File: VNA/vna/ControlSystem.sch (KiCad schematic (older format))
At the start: 2 parts

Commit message: block diagram for presentation completed
at this stage i have completed the overall block diagram for the initial presentation.

the blocks are mostly empty and require further development. the overall block diagram neglects power supply connections for clarity, these will be added internal to the blocks.
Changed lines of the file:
@@
 $Descr A4 11693 8268
 encoding utf-8
-Sheet 8 9
+Sheet 10 10
 Title ""
 Date ""
@@
 Text HLabel 6650 1500 1    50   Input ~ 0
 Aref
+Text HLabel 4800 2000 0    50   Input ~ 0
+VmagIn
+Text HLabel 4800 2200 0    50   Input ~ 0
+VphaseIn
+Text HLabel 4800 2450 0    50   Input ~ 0
+VrefIn
+Text HLabel 4800 2650 0    50   Input ~ 0
+DataNegIn
+Text HLabel 4800 2900 0    50   Input ~ 0
+DataPosIn
+Text HLabel 4800 3150 0    50   Input ~ 0
+SrcCtlOut
+Text HLabel 4800 3300 0    50   Input ~ 0
+ACtrlOut
+Text HLabel 4800 3450 0    50   Input ~ 0
+BCtrlOut
+Text HLabel 4800 1750 0    50   Input ~ 0
+RFControl
 $EndSCHEMATC

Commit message: adjusted main schematic to suit initial presentation
i moved a few blocks around so that the cropped version of the block diagram would fit nicely in my semester 1 presentation
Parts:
- gave numbers to parts that had none: 2
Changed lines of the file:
@@
 The design for this control system is based upon the open hardware of the arduino.\nadapted from electronoobs design\nhttp://www.electronoobs.com/eng_arduino_tut31_sch3.php
 $Comp
-L MCU_Microchip_ATmega:ATmega328PB-AU U?
+L MCU_Microchip_ATmega:ATmega328PB-AU U2
 U 1 1 5CD24AD6
 P 7450 2700
-F 0 "U?" H 7350 2850 50  0000 C CNN
+F 0 "U2" H 7350 2850 50  0000 C CNN
 F 1 "ATmega328PB-AU" H 7350 3050 50  0000 C CNN
 F 2 "Package_QFP:TQFP-32_7x7mm_P0.8mm" H 7450 2700 50  0001 C CIN
@@
 	7450 1200 7550 1200
 $Comp
-L power:GNDA #PWR?
+L power:GNDA #PWR022
 U 1 1 5CD27167
 P 6250 1650
-F 0 "#PWR?" H 6250 1400 50  0001 C CNN
+F 0 "#PWR022" H 6250 1400 50  0001 C CNN
 F 1 "GNDA" H 6255 1477 50  0000 C CNN
 F 2 "" H 6250 1650 50  0001 C CNN
@@
 $EndComp
 $Comp
-L Device:C_Small C?
+L Device:C_Small C12
 U 1 1 5CD27A26
 P 6350 1500
-F 0 "C?" V 6121 1500 50  0000 C CNN
+F 0 "C12" V 6121 1500 50  0000 C CNN
 F 1 "100n" V 6212 1500 50  0000 C CNN
 F 2 "" H 6350 1500 50  0001 C CNN

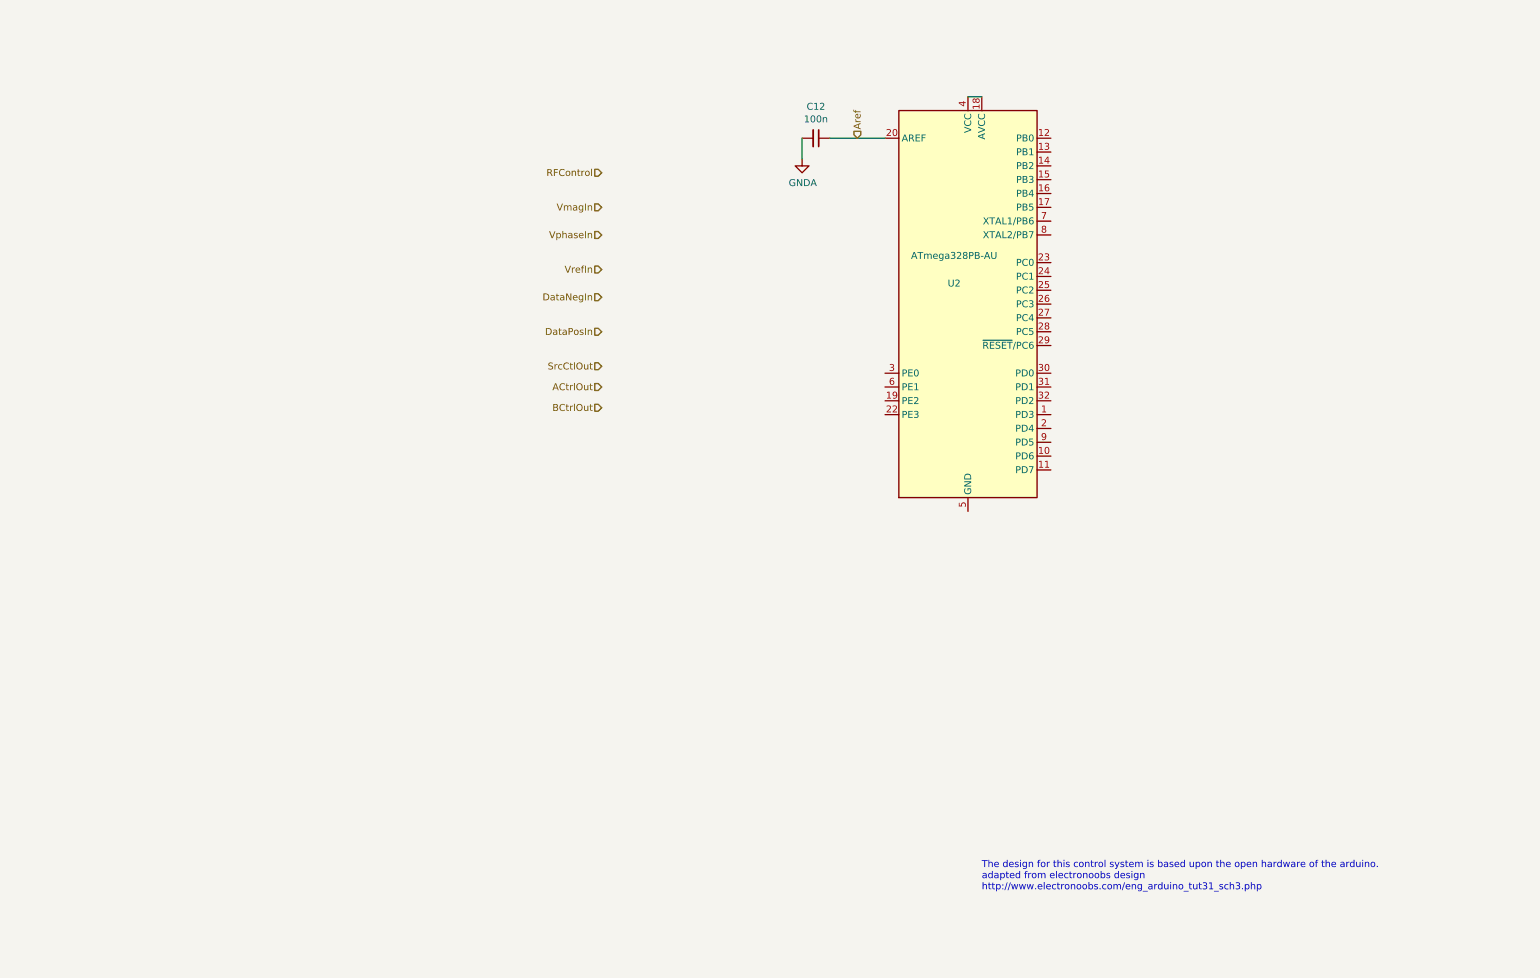
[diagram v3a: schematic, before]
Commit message: micro-controller pins labelled
micro controller pins have been labelled, the pins on the bottom are yet to be linked to them.

still to wire up ftdi chip,

still to decide upon rf switch control schema.
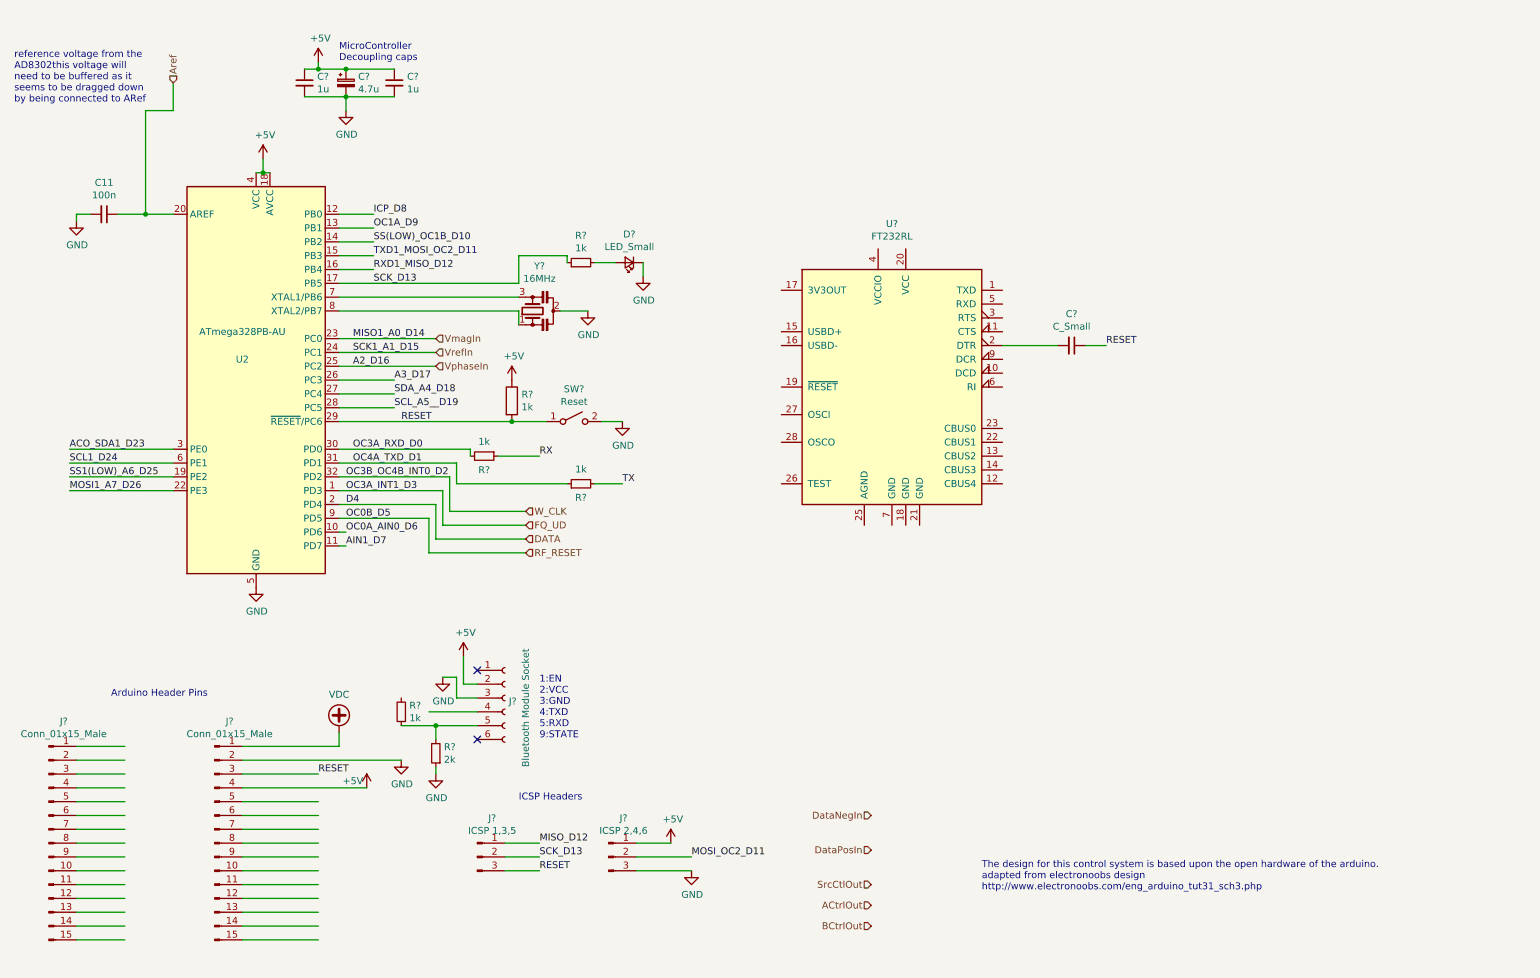
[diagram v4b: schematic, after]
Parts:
- added C? (x2): 1u, symbol Device:C_Small
- added C?: 4.7u, symbol Device:CP_Small
- added C?: C_Small, symbol Device:C_Small
- added D?: LED_Small, symbol Device:LED_Small
- added J?: Bluetooth Module Socket, symbol Connector:Conn_01x06_Female
- added J? (x2): Conn_01x15_Male, symbol Connector:Conn_01x15_Male
- added J?: ICSP 1,3,5, symbol Connector:Conn_01x03_Male
- added J?: ICSP 2,4,6, symbol Connector:Conn_01x03_Male
- added R?: 1k, symbol Device:R
- added R?: 2k, symbol Device:R_Small
- added R? (x4): 1k, symbol Device:R_Small
- added SW?: Reset, symbol Switch:SW_SPST
- added U?: FT232RL, Package_SO:SSOP-28_5.3x10.2mm_P0.65mm, symbol Interface_USB:FT232RL
- added Y?: 16MHz, symbol Device:Resonator_Small
- renumbered C12 to C11
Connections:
- net labels added: +5V, A2_D16, A3_D17, ACO_SDA1_D23, AIN1_D7, D4, DATA, FQ_UD, GND, ICP_D8, MISO1_A0_D14, MISO_D12, MOSI1_A7_D26, MOSI_OC2_D11, OC0A_AIN0_D6, OC0B_D5, OC1A_D9, OC3A_INT1_D3, OC3A_RXD_D0, OC3B_OC4B_INT0_D2, OC4A_TXD_D1, RESET, RF_RESET, RX, RXD1_MISO_D12, SCK1_A1_D15, SCK_D13, SCL1_D24, SCL_A5__D19, SDA_A4_D18, SS(LOW)_OC1B_D10, SS1(LOW)_A6_D25, TX, TXD1_MOSI_OC2_D11, VDC, W_CLK
- net labels removed: GNDA, RFControl
- wire segments 3 -> 115
- no-connect marks 0 -> 2
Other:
- note added: "1:EN\n2:VCC\n3:GND\n4:TXD\n5:RXD\n9:STATE"
- note added: "Arduino Header Pins"
- note added: "ICSP Headers"
- note added: "MicroController\nDecoupling caps"
- note added: "reference voltage from the \nAD8302this voltage will \nneed to be buffered as it \nseems to be dragged down \nby being connected to ARef"
- moved on the sheet: C11, U2

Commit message: finished controller, chose compatible switches
controller and rf switches have been completed.

ToDo: finish filter design for RF Source, add auto gain control
ToDo: finish directional coupler footprints
ToDo: PCB Layout
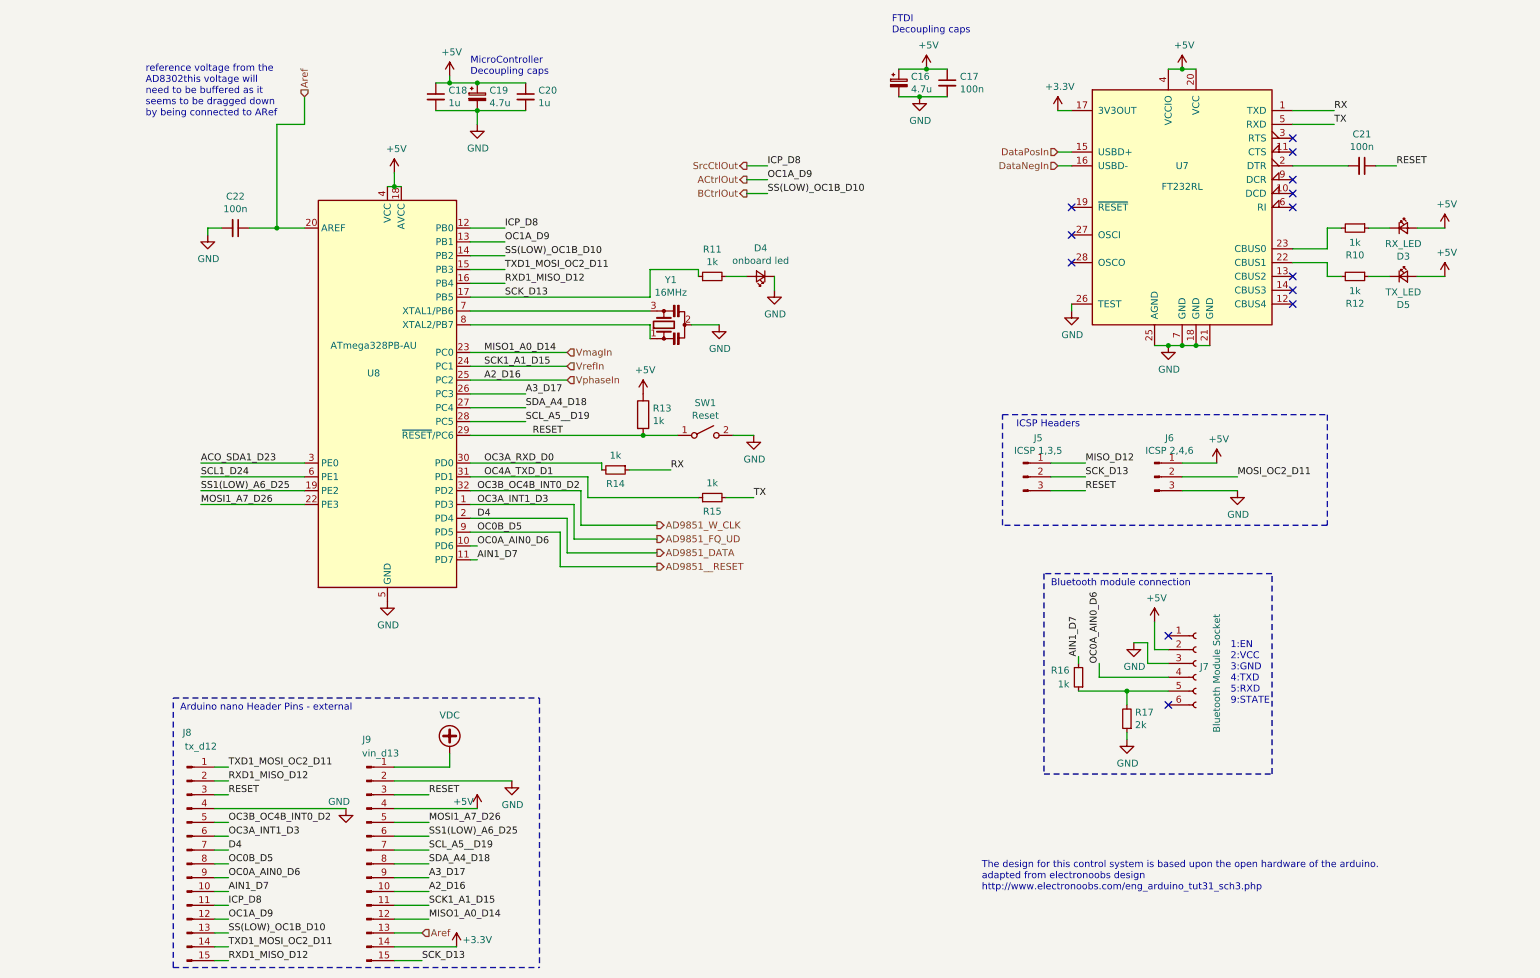
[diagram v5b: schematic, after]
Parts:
- added C16: 4.7u, Capacitor_SMD:CP_Elec_6.3x5.4_Nichicon, symbol Device:CP_Small
- added C17: 100n, Capacitor_SMD:C_0805_2012Metric_Pad1.15x1.40mm_HandSolder, symbol Device:C_Small
- added D3: RX_LED, LED_SMD:LED_0805_2012Metric, symbol Device:LED_Small
- added D5: TX_LED, LED_SMD:LED_0805_2012Metric, symbol Device:LED_Small
- added R10, R12: 1k, Resistor_SMD:R_0805_2012Metric_Pad1.15x1.40mm_HandSolder, symbol Device:R_Small
- C18, C20: renamed from C?; footprint (none) -> Capacitor_SMD:C_0805_2012Metric_Pad1.15x1.40mm_HandSolder
- C19: renamed from C?; footprint (none) -> Capacitor_SMD:CP_Elec_6.3x5.4_Nichicon
- C21: renamed from C?; value C_Small -> 100n; footprint (none) -> Capacitor_SMD:C_0805_2012Metric_Pad1.15x1.40mm_HandSolder
- C22: renamed from C11; footprint (none) -> Capacitor_SMD:C_0805_2012Metric_Pad1.15x1.40mm_HandSolder
- D4: renamed from D?; value LED_Small -> onboard led; footprint (none) -> LED_SMD:LED_0805_2012Metric
- J5, J6: renamed from J?; footprint (none) -> Connector_PinHeader_2.54mm:PinHeader_1x03_P2.54mm_Vertical
- J7: renamed from J?; footprint (none) -> Connector_PinSocket_2.54mm:PinSocket_1x06_P2.54mm_Vertical
- J8: renamed from J?; value Conn_01x15_Male -> tx_d12; footprint (none) -> Connector_PinSocket_2.54mm:PinSocket_1x12_P2.54mm_Vertical
- J9: renamed from J?; value Conn_01x15_Male -> vin_d13; footprint (none) -> Connector_PinSocket_2.54mm:PinSocket_1x12_P2.54mm_Vertical
- R11, R13, R14, R15, R16, R17: renamed from R?; footprint (none) -> Resistor_SMD:R_0805_2012Metric_Pad1.15x1.40mm_HandSolder
- Y1: renamed from Y?; footprint (none) -> Crystal:Crystal_SMD_TXC_7A-2Pin_5x3.2mm
- gave numbers to parts that had none: 2
- renumbered U2 to U8
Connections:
- net labels added: +3.3V, AD9851_DATA, AD9851_FQ_UD, AD9851_W_CLK, AD9851__RESET
- net labels removed: DATA, FQ_UD, RF_RESET, W_CLK
- wire segments 115 -> 146
- no-connect marks 2 -> 13
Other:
- note added: "Arduino nano Header Pins - external"
- note added: "Bluetooth module connection"
- note added: "FTDI\nDecoupling caps"
- note removed: "Arduino Header Pins"
- moved on the sheet: C18, C19, C20, C21, C22, D4, J5, J6, J7, J8, J9, R11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

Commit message: custom footprint for couplers, added decoupling caps
added custom footprint for directional couplers - will need to verify it

added decoupling caps to ad9851
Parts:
- removed Y1: 16MHz, Crystal:Crystal_SMD_TXC_7A-2Pin_5x3.2mm, symbol Device:Resonator_Small
- added C26, C27: C0G 22p, Capacitor_SMD:C_1206_3216Metric_Pad1.42x1.75mm_HandSolder, symbol Device:C_Small
- added Y1: 16MHz, Crystal:Crystal_HC18-U_Vertical, symbol Device:Crystal_Small
- C17, C18, C20, C21, C22: footprint Capacitor_SMD:C_0805_2012Metric_Pad1.15x1.40mm_HandSolder -> Capacitor_SMD:C_1206_3216Metric_Pad1.42x1.75mm_HandSolder
- R10, R11, R12, R13, R14, R15, R16, R17: footprint Resistor_SMD:R_0805_2012Metric_Pad1.15x1.40mm_HandSolder -> Resistor_SMD:R_1206_3216Metric_Pad1.42x1.75mm_HandSolder
- SW1: footprint (none) -> Button_Switch_SMD:SW_SPST_FSMSM
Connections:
- net GND: now also C26.1, C27.1
- net at U8.7 (XTAL1/PB6): now also C26.2, Y1.1
- net at U8.8 (XTAL2/PB7): now also C27.2, Y1.2
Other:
- note added: "ATMEGA328P\nDecoupling caps"
- note removed: "MicroController\nDecoupling caps"
- moved on the sheet: C16, C17, C21, D3, D5, J5, J6, J7, R10, R12, R16, R17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

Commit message: beginning pcb layout
pcb layout process begun
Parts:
- J8, J9: footprint Connector_PinSocket_2.54mm:PinSocket_1x12_P2.54mm_Vertical -> Connector_PinSocket_2.54mm:PinSocket_1x15_P2.54mm_Vertical
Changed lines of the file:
@@
 F 0 "J8" H 1800 7700 50  0000 C CNN
 F 1 "tx_d12" H 1900 7600 50  0000 C CNN
-F 2 "Connector_PinSocket_2.54mm:PinSocket_1x12_P2.54mm_Vertical" H 1800 6750 50  0001 C CNN
+F 2 "Connector_PinSocket_2.54mm:PinSocket_1x15_P2.54mm_Vertical" H 1800 6750 50  0001 C CNN
 F 3 "~" H 1800 6750 50  0001 C CNN
 	1    1800 6750
@@
 F 0 "J9" H 3100 7650 50  0000 C CNN
 F 1 "vin_d13" H 3200 7550 50  0000 C CNN
-F 2 "Connector_PinSocket_2.54mm:PinSocket_1x12_P2.54mm_Vertical" H 3100 6750 50  0001 C CNN
+F 2 "Connector_PinSocket_2.54mm:PinSocket_1x15_P2.54mm_Vertical" H 3100 6750 50  0001 C CNN
 F 3 "~" H 3100 6750 50  0001 C CNN
 	1    3100 6750
